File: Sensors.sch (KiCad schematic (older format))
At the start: 66 parts, among them U1 MPXH6250A, U6 SP720

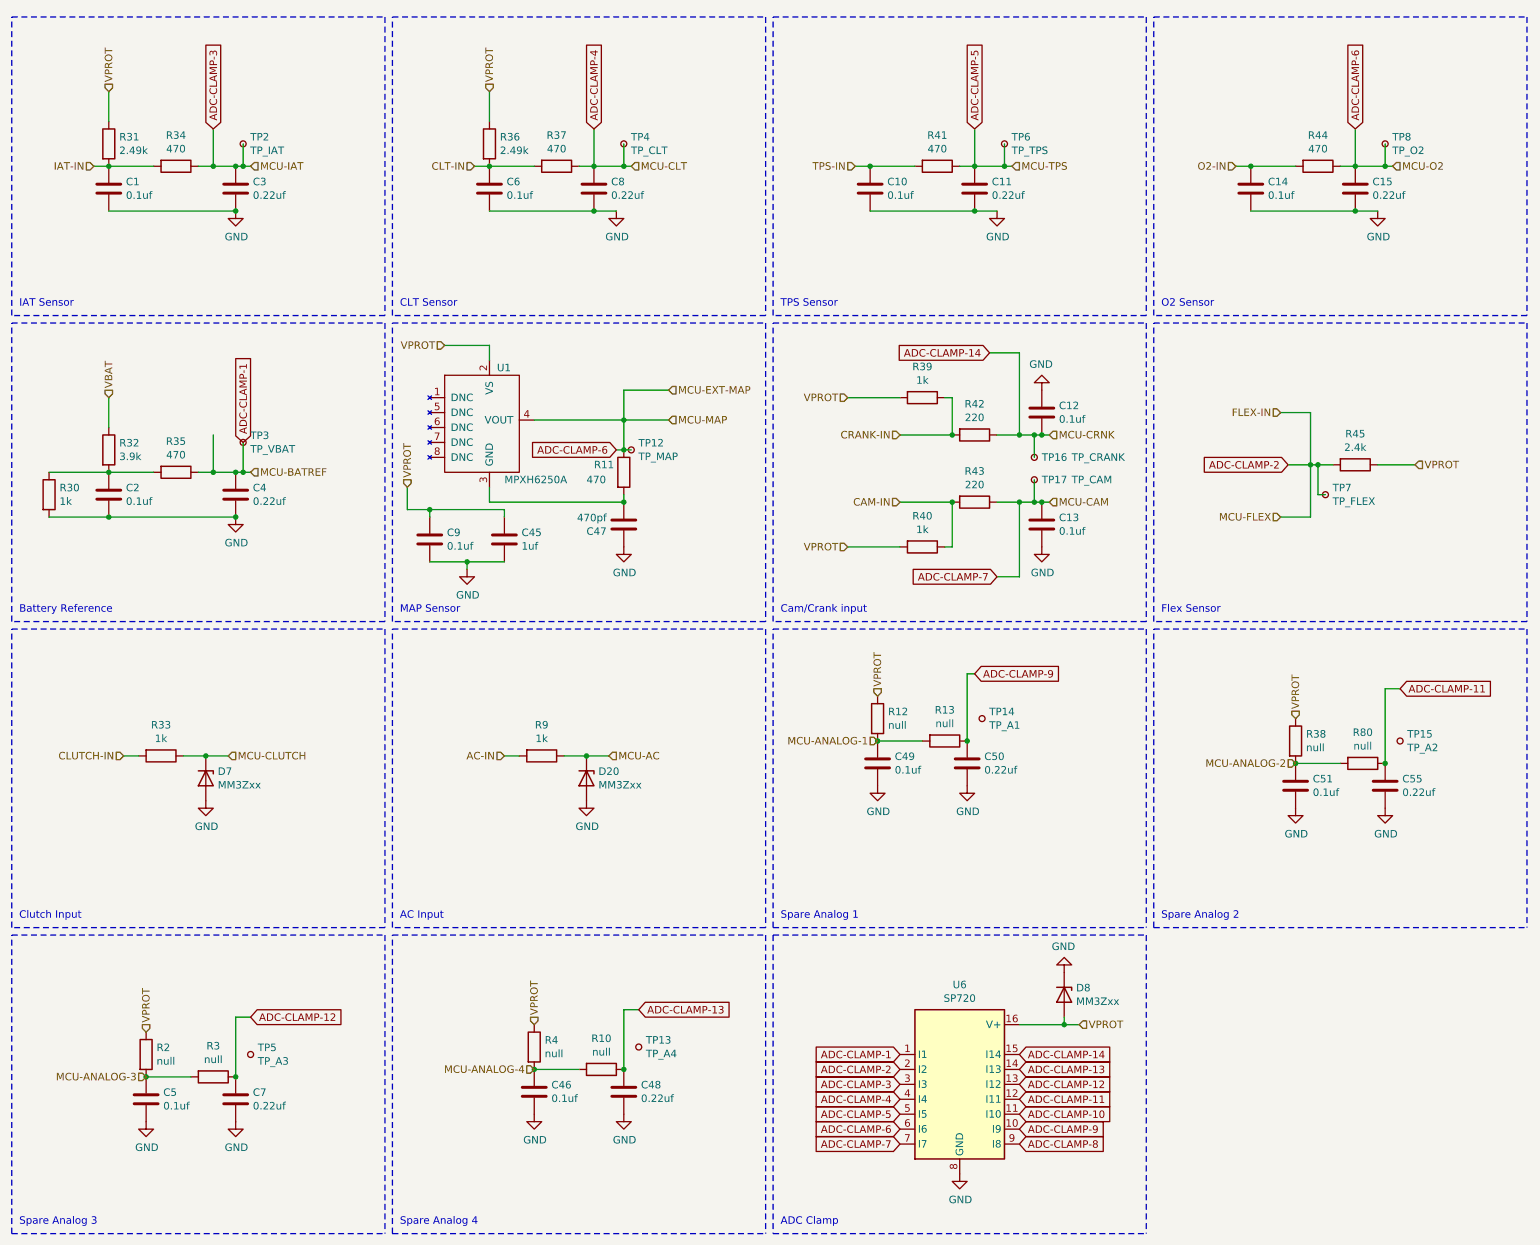
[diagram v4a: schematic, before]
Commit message: Layout checkpoint: everything fits on the board
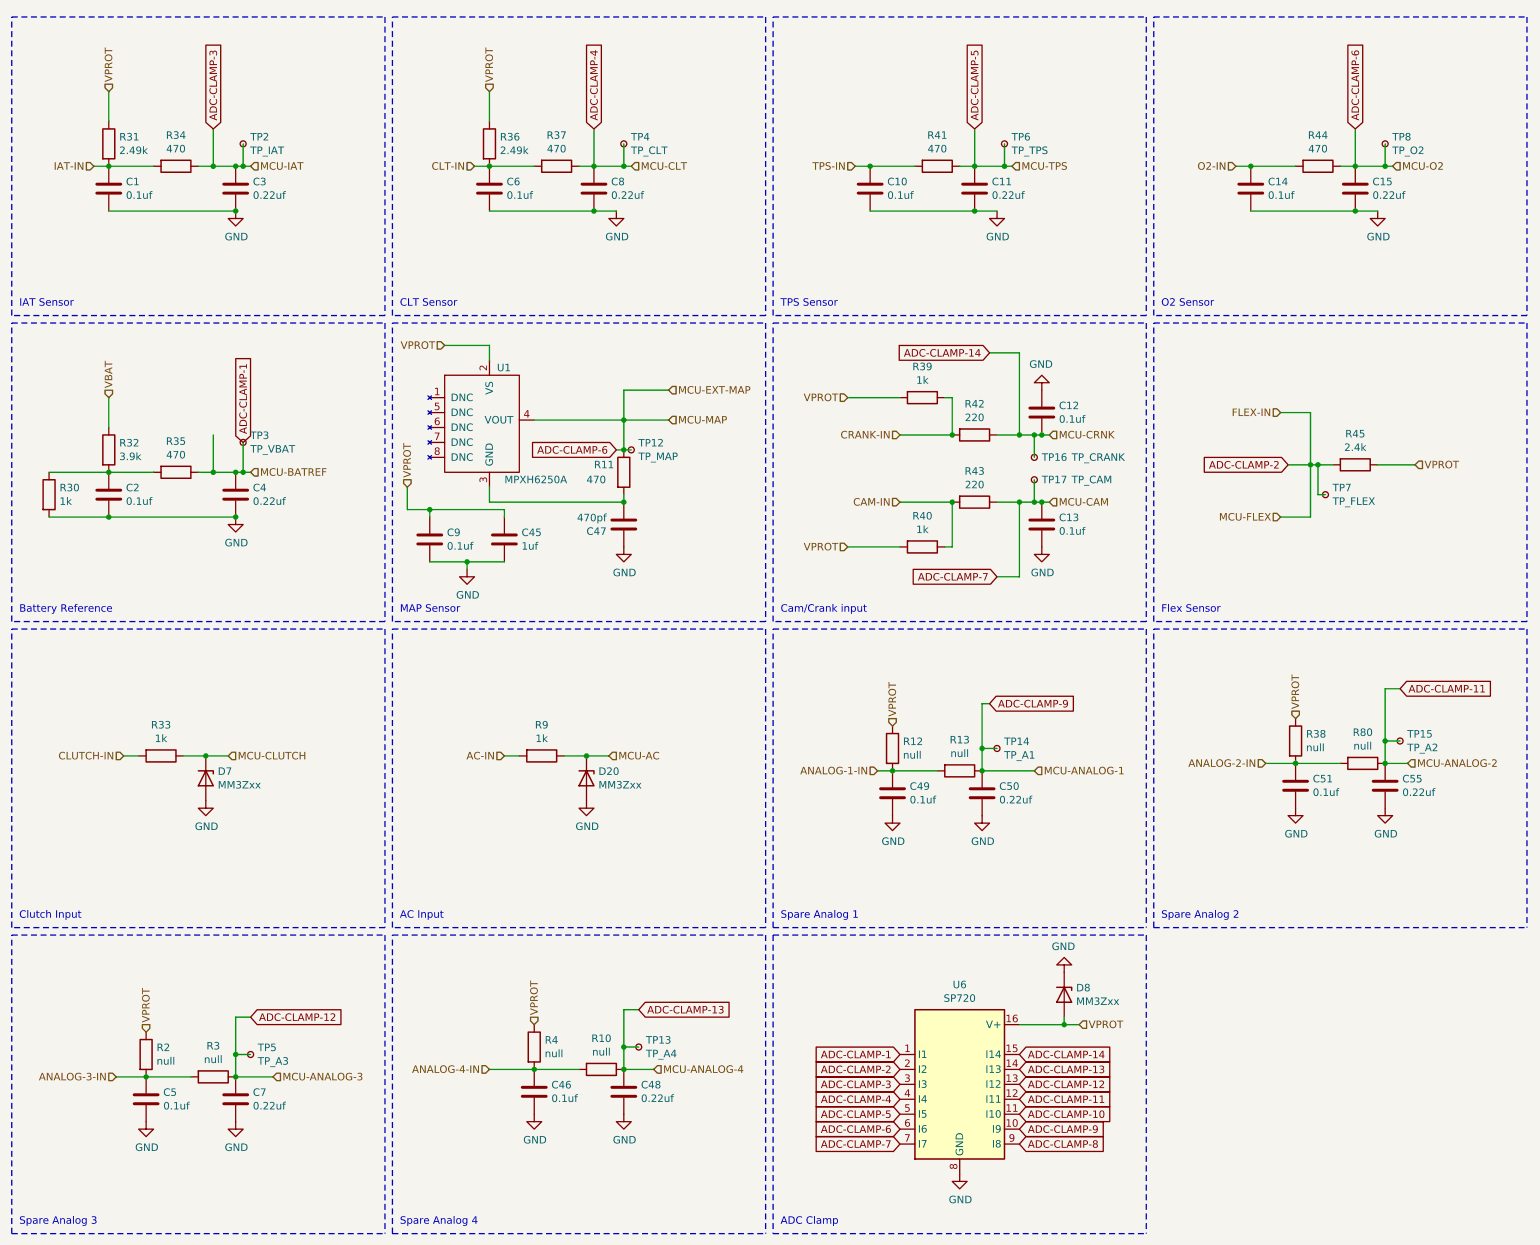
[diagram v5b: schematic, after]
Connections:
- net ADC-CLAMP-11: now also TP15.1
- net ADC-CLAMP-12: now also TP5.1
- net ADC-CLAMP-13: now also TP13.1
- net ADC-CLAMP-9: now also TP14.1
- net MCU-ANALOG-1 renamed ANALOG-1-IN
- net MCU-ANALOG-2 renamed ANALOG-2-IN
- net MCU-ANALOG-3 renamed ANALOG-3-IN
- net MCU-ANALOG-4 renamed ANALOG-4-IN
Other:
- moved on the sheet: C49, C50, R12, R13, TP14
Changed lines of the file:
@@
 Text HLabel 6450 3750 0    50   Input ~ 0
 CAM-IN
-Text GLabel 6950 4900 2    50   Input ~ 0
+Text GLabel 7050 5100 2    50   Input ~ 0
 ADC-CLAMP-9
 Text HLabel 7450 3750 2    50   Input ~ 0
@@
 Wire Notes Line
 	5600 6650 8100 6650
-Text HLabel 6300 5050 1    50   Input ~ 0
+Text HLabel 6400 5250 1    50   Input ~ 0
 VPROT
 $Comp
 L Device:R R12
 U 1 1 61DD1503
-P 6300 5200
-F 0 "R12" H 6370 5246 50  0000 L CNN
-F 1 "null" H 6370 5155 50  0000 L CNN
-F 2 "Resistor_SMD:R_0805_2012Metric_Pad1.20x1.40mm_HandSolder" V 6230 5200 50  0001 C CNN
-F 3 "~" H 6300 5200 50  0001 C CNN
-F 4 "YAG1854CT-ND" H 6300 5200 50  0001 C CNN "DIGIKEY"
-F 5 "C21237" H 6300 5200 50  0001 C CNN "LCSC_PN"
-F 6 "0805" H 6300 5200 50  0001 C CNN "LCSC_FP"
-	1    6300 5200
+P 6400 5400
+F 0 "R12" H 6470 5446 50  0000 L CNN
+F 1 "null" H 6470 5355 50  0000 L CNN
+F 2 "Resistor_SMD:R_0805_2012Metric_Pad1.20x1.40mm_HandSolder" V 6330 5400 50  0001 C CNN
+F 3 "~" H 6400 5400 50  0001 C CNN
+F 4 "YAG1854CT-ND" H 6400 5400 50  0001 C CNN "DIGIKEY"
+F 5 "C21237" H 6400 5400 50  0001 C CNN "LCSC_PN"
+F 6 "0805" H 6400 5400 50  0001 C CNN "LCSC_FP"
+	1    6400 5400
 	1    0    0    -1
 $EndComp
@@
 L Device:C C?
 U 1 1 61DD56EB
-P 6300 5500
+P 6400 5700
 AR Path="/5F2F8F45/61DD56EB" Ref="C?"  Part="1"
 AR Path="/5EFFD74E/61DD56EB" Ref="C49"  Part="1"
-F 0 "C49" H 6415 5546 50  0000 L CNN
-F 1 "0.1uf" H 6415 5455 50  0000 L CNN
-F 2 "Capacitor_SMD:C_0805_2012Metric_Pad1.18x1.45mm_HandSolder" H 6338 5350 50  0001 C CNN
-F 3 "https://datasheet.lcsc.com/szlcsc/YAGEO-CC0805KRX7R9BB104_C49678.pdf" H 6300 5500 50  0001 C CNN
-F 4 "311-1140-1-ND" H 6300 5500 50  0001 C CNN "DIGIKEY"
-F 5 "603-CC805KRX7R9BB104" H 6300 5500 50  0001 C CNN "MOUSER"
-F 6 "C49678" H 6300 5500 50  0001 C CNN "LCSC_PN"
-F 7 "0805" H 6300 5500 50  0001 C CNN "LCSC_FP"
-	1    6300 5500
+F 0 "C49" H 6515 5746 50  0000 L CNN
+F 1 "0.1uf" H 6515 5655 50  0000 L CNN
+F 2 "Capacitor_SMD:C_0805_2012Metric_Pad1.18x1.45mm_HandSolder" H 6438 5550 50  0001 C CNN
+F 3 "https://datasheet.lcsc.com/szlcsc/YAGEO-CC0805KRX7R9BB104_C49678.pdf" H 6400 5700 50  0001 C CNN
+F 4 "311-1140-1-ND" H 6400 5700 50  0001 C CNN "DIGIKEY"
+F 5 "603-CC805KRX7R9BB104" H 6400 5700 50  0001 C CNN "MOUSER"
+F 6 "C49678" H 6400 5700 50  0001 C CNN "LCSC_PN"
+F 7 "0805" H 6400 5700 50  0001 C CNN "LCSC_FP"
+	1    6400 5700
 	1    0    0    -1
 $EndComp
@@
 L Device:R R13
 U 1 1 61DD95EE
-P 6750 5350
-F 0 "R13" V 6543 5350 50  0000 C CNN
-F 1 "null" V 6634 5350 50  0000 C CNN
-F 2 "Resistor_SMD:R_0805_2012Metric_Pad1.20x1.40mm_HandSolder" V 6680 5350 50  0001 C CNN
-F 3 "~" H 6750 5350 50  0001 C CNN
-F 4 "P470CCT-ND" V 6750 5350 50  0001 C CNN "DIGIKEY"
-F 5 "C17710" V 6750 5350 50  0001 C CNN "LCSC_PN"
-F 6 "0805" V 6750 5350 50  0001 C CNN "LCSC_FP"
-	1    6750 5350
+P 6850 5550
+F 0 "R13" V 6643 5550 50  0000 C CNN
+F 1 "null" V 6734 5550 50  0000 C CNN
+F 2 "Resistor_SMD:R_0805_2012Metric_Pad1.20x1.40mm_HandSolder" V 6780 5550 50  0001 C CNN
+F 3 "~" H 6850 5550 50  0001 C CNN
+F 4 "P470CCT-ND" V 6850 5550 50  0001 C CNN "DIGIKEY"
+F 5 "C17710" V 6850 5550 50  0001 C CNN "LCSC_PN"
+F 6 "0805" V 6850 5550 50  0001 C CNN "LCSC_FP"
+	1    6850 5550
 	0    1    1    0
 $EndComp
@@
 L Device:C C50
 U 1 1 61DDE5C4
-P 6900 5500
-F 0 "C50" H 7015 5546 50  0000 L CNN
-F 1 "0.22uf" H 7015 5455 50  0000 L CNN
-F 2 "Capacitor_SMD:C_0805_2012Metric_Pad1.18x1.45mm_HandSolder" H 6938 5350 50  0001 C CNN
-F 3 "~" H 6900 5500 50  0001 C CNN
-F 4 "1276-1284-1-ND" H 6900 5500 50  0001 C CNN "DIGIKEY"
-F 5 "C5378" H 6900 5500 50  0001 C CNN "LCSC_PN"
-F 6 "0805" H 6900 5500 50  0001 C CNN "LCSC_FP"
-	1    6900 5500
-	1    0    0    -1
-$EndComp
-Wire Wire Line
-	6600 5350 6300 5350
-Connection ~ 6300 5350
-Text HLabel 6300 5350 0    50   Input ~ 0
+P 7000 5700
+F 0 "C50" H 7115 5746 50  0000 L CNN
+F 1 "0.22uf" H 7115 5655 50  0000 L CNN
+F 2 "Capacitor_SMD:C_0805_2012Metric_Pad1.18x1.45mm_HandSolder" H 7038 5550 50  0001 C CNN
+F 3 "~" H 7000 5700 50  0001 C CNN
+F 4 "1276-1284-1-ND" H 7000 5700 50  0001 C CNN "DIGIKEY"
+F 5 "C5378" H 7000 5700 50  0001 C CNN "LCSC_PN"
+F 6 "0805" H 7000 5700 50  0001 C CNN "LCSC_FP"
+	1    7000 5700
+	1    0    0    -1
+$EndComp
+Wire Wire Line
+	6700 5550 6400 5550
+Connection ~ 6400 5550
+Text HLabel 7350 5550 2    50   Input ~ 0
 MCU-ANALOG-1
 $Comp
 L power:GND #PWR033
 U 1 1 61DF4E3D
-P 6300 5650
-F 0 "#PWR033" H 6300 5400 50  0001 C CNN
-F 1 "GND" H 6305 5477 50  0000 C CNN
-F 2 "" H 6300 5650 50  0001 C CNN
-F 3 "" H 6300 5650 50  0001 C CNN
-	1    6300 5650
+P 6400 5850
+F 0 "#PWR033" H 6400 5600 50  0001 C CNN
+F 1 "GND" H 6405 5677 50  0000 C CNN
+F 2 "" H 6400 5850 50  0001 C CNN
+F 3 "" H 6400 5850 50  0001 C CNN
+	1    6400 5850
 	1    0    0    -1
 $EndComp
@@
 L power:GND #PWR055
 U 1 1 61DF51AD
-P 6900 5650
-F 0 "#PWR055" H 6900 5400 50  0001 C CNN
-F 1 "GND" H 6905 5477 50  0000 C CNN
-F 2 "" H 6900 5650 50  0001 C CNN
-F 3 "" H 6900 5650 50  0001 C CNN
-	1    6900 5650
+P 7000 5850
+F 0 "#PWR055" H 7000 5600 50  0001 C CNN
+F 1 "GND" H 7005 5677 50  0000 C CNN
+F 2 "" H 7000 5850 50  0001 C CNN
+F 3 "" H 7000 5850 50  0001 C CNN
+	1    7000 5850
 	1    0    0    -1
 $EndComp
@@
 L Connector:TestPoint_Small TP14
 U 1 1 61DF6FD5
-P 7000 5200
-F 0 "TP14" H 7048 5246 50  0000 L CNN
-F 1 "TP_A1" H 7048 5155 50  0000 L CNN
-F 2 "TestPoint:TestPoint_Pad_D1.0mm" H 7200 5200 50  0001 C CNN
-F 3 "~" H 7200 5200 50  0001 C CNN
-	1    7000 5200
+P 7100 5400
+F 0 "TP14" H 7148 5446 50  0000 L CNN
+F 1 "TP_A1" H 7148 5355 50  0000 L CNN
+F 2 "TestPoint:TestPoint_Pad_D1.0mm" H 7300 5400 50  0001 C CNN
+F 3 "~" H 7300 5400 50  0001 C CNN
+	1    7100 5400
 	1    0    0    -1
 $EndComp
@@
 	9400 5500 9100 5500
 Connection ~ 9100 5500
-Text HLabel 9100 5500 0    50   Input ~ 0
+Text HLabel 9850 5500 2    50   Input ~ 0
 MCU-ANALOG-2
 $Comp
@@
 	1700 7600 1400 7600
 Connection ~ 1400 7600
-Text HLabel 1400 7600 0    50   Input ~ 0
+Text HLabel 2250 7600 2    50   Input ~ 0
 MCU-ANALOG-3
 $Comp
@@
 	4300 7550 4000 7550
 Connection ~ 4000 7550
-Text HLabel 4000 7550 0    50   Input ~ 0
+Text HLabel 4800 7550 2    50   Input ~ 0
 MCU-ANALOG-4
 $Comp
@@
 ADC-CLAMP-7
 Wire Wire Line
-	6950 4900 6900 4900
-Wire Wire Line
-	6900 4900 6900 5350
-Connection ~ 6900 5350
+	7050 5100 7000 5100
+Wire Wire Line
+	7000 5100 7000 5400
+Connection ~ 7000 5550
 Text GLabel 9800 5000 2    50   Input ~ 0
 ADC-CLAMP-11
@@
 	9800 5000 9700 5000
 Wire Wire Line
-	9700 5000 9700 5500
+	9700 5000 9700 5350
 Connection ~ 9700 5500
 Text GLabel 2100 7200 2    50   Input ~ 0
@@
 	2100 7200 2000 7200
 Wire Wire Line
-	2000 7200 2000 7600
+	2000 7200 2000 7450
 Connection ~ 2000 7600
 Text GLabel 4700 7150 2    50   Input ~ 0
@@
 	4700 7150 4600 7150
 Wire Wire Line
-	4600 7150 4600 7550
+	4600 7150 4600 7400
 Connection ~ 4600 7550
 Text GLabel 9500 1250 1    50   Input ~ 0
@@
 Text GLabel 7050 2750 0    50   Input ~ 0
 ADC-CLAMP-14
+Wire Wire Line
+	2100 7450 2000 7450
+Connection ~ 2000 7450
+Wire Wire Line
+	2000 7450 2000 7600
+Wire Wire Line
+	2250 7600 2000 7600
+Text HLabel 1200 7600 0    50   Input ~ 0
+ANALOG-3-IN
+Wire Wire Line
+	1200 7600 1400 7600
+Wire Wire Line
+	4700 7400 4600 7400
+Connection ~ 4600 7400
+Wire Wire Line
+	4600 7400 4600 7550
+Wire Wire Line
+	4600 7550 4800 7550
+Text HLabel 3700 7550 0    50   Input ~ 0
+ANALOG-4-IN
+Wire Wire Line
+	3700 7550 4000 7550
+Wire Wire Line
+	7350 5550 7000 5550
+Wire Wire Line
+	7000 5400 7100 5400
+Connection ~ 7000 5400
+Wire Wire Line
+	7000 5400 7000 5550
+Text HLabel 6300 5550 0    50   Input ~ 0
+ANALOG-1-IN
+Wire Wire Line
+	6300 5550 6400 5550
+Wire Wire Line
+	9700 5500 9850 5500
+Wire Wire Line
+	9800 5350 9700 5350
+Connection ~ 9700 5350
+Wire Wire Line
+	9700 5350 9700 5500
+Text HLabel 8900 5500 0    50   Input ~ 0
+ANALOG-2-IN
+Wire Wire Line
+	8900 5500 9100 5500
 $EndSCHEMATC

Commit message: Finish reroute again
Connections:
- net ADC-CLAMP-1: now also C50.1, R13.1, TP14.1; no longer C4.1, R35.1, TP3.1
- net ADC-CLAMP-10: now also C8.1, R37.1, TP4.1
- net ADC-CLAMP-11: now also C15.1, R44.1, TP8.1; no longer C55.1, R80.1, TP15.1
- net ADC-CLAMP-12: now also C4.1, R35.1, TP3.1; no longer C7.1, R3.1, TP5.1
- net ADC-CLAMP-13: now also C3.1, R34.1, TP2.1; no longer C48.1, R10.1, TP13.1
- net ADC-CLAMP-14: now also C11.1, R41.1, TP6.1; no longer C12.2, R42.1, TP16.1
- net ADC-CLAMP-2: now also C55.1, R80.1, TP15.1; no longer R45.2, TP7.1
- net ADC-CLAMP-3: now also C7.1, R3.1, TP5.1; no longer C3.1, R34.1, TP2.1
- net ADC-CLAMP-4: now also C48.1, R10.1, TP13.1; no longer C8.1, R37.1, TP4.1
- net ADC-CLAMP-5: now also C12.2, R42.1, TP16.1; no longer C11.1, R41.1, TP6.1
- net ADC-CLAMP-6: now also C13.1, R43.1, TP17.1; no longer C15.1, R11.1, R44.1, TP12.1, TP8.1, U1.4 (VOUT)
- net ADC-CLAMP-7: now also R45.2, TP7.1; no longer C13.1, R43.1, TP17.1
- net ADC-CLAMP-9: now also R11.1, TP12.1, U1.4 (VOUT); no longer C50.1, R13.1, TP14.1
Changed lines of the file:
@@
 Text GLabel 6450 7450 0    50   Input ~ 0
 ADC-CLAMP-1
-Text GLabel 2050 3350 1    50   Input ~ 0
-ADC-CLAMP-1
+Text GLabel 1850 3300 1    50   Input ~ 0
+ADC-CLAMP-12
 Wire Wire Line
 	1850 1250 1850 1500
@@
 	4300 1500 4400 1500
 Text GLabel 9050 3500 0    50   Input ~ 0
-ADC-CLAMP-2
+ADC-CLAMP-7
 Wire Wire Line
 	4400 1250 4400 1500
@@
 	6850 1500 6950 1500
 Text GLabel 1850 1250 1    50   Input ~ 0
-ADC-CLAMP-3
+ADC-CLAMP-13
 Wire Wire Line
 	6950 1250 6950 1500
@@
 	9400 1500 9500 1500
 Text GLabel 4400 1250 1    50   Input ~ 0
-ADC-CLAMP-4
+ADC-CLAMP-10
 Wire Wire Line
 	9500 1250 9500 1500
@@
 	1750 3550 1850 3550
 Text GLabel 6950 1250 1    50   Input ~ 0
-ADC-CLAMP-5
+ADC-CLAMP-14
 Wire Wire Line
 	1850 3300 1850 3550
@@
 Text HLabel 6450 3750 0    50   Input ~ 0
 CAM-IN
-Text GLabel 7050 5100 2    50   Input ~ 0
-ADC-CLAMP-9
 Text HLabel 7450 3750 2    50   Input ~ 0
 MCU-CAM
@@
 F 3 "~" H 7550 3600 50  0001 C CNN
 	1    7350 3600
-	1    0    0    -1
+	1    0    0    1
 $EndComp
 Wire Wire Line
@@
 	4600 3700 4600 3750
 Text GLabel 4550 3400 0    50   Input ~ 0
-ADC-CLAMP-6
+ADC-CLAMP-9
 Text HLabel 4900 3200 2    50   Input ~ 0
 MCU-MAP
@@
 Wire Wire Line
 	4650 3400 4600 3400
-Text HLabel 4900 3000 2    50   Input ~ 0
-MCU-EXT-MAP
 $Comp
 L Device:C C?
@@
 Connection ~ 4600 3200
 Wire Wire Line
-	4900 3000 4600 3000
-Wire Wire Line
-	4600 3000 4600 3200
-Wire Wire Line
 	3400 2700 3700 2700
 Wire Wire Line
@@
 Connection ~ 3300 3800
 Text GLabel 7100 4250 0    50   Input ~ 0
-ADC-CLAMP-7
+ADC-CLAMP-6
 Wire Wire Line
 	7050 5100 7000 5100
@@
 Connection ~ 7000 5550
 Text GLabel 9800 5000 2    50   Input ~ 0
-ADC-CLAMP-11
+ADC-CLAMP-2
 Wire Wire Line
 	9800 5000 9700 5000
@@
 Connection ~ 9700 5500
 Text GLabel 2100 7200 2    50   Input ~ 0
-ADC-CLAMP-12
+ADC-CLAMP-3
 Wire Wire Line
 	2100 7200 2000 7200
@@
 Connection ~ 2000 7600
 Text GLabel 4700 7150 2    50   Input ~ 0
-ADC-CLAMP-13
+ADC-CLAMP-4
 Wire Wire Line
 	4700 7150 4600 7150
@@
 Connection ~ 4600 7550
 Text GLabel 9500 1250 1    50   Input ~ 0
-ADC-CLAMP-6
+ADC-CLAMP-11
 Text GLabel 7050 2750 0    50   Input ~ 0
-ADC-CLAMP-14
+ADC-CLAMP-5
 Wire Wire Line
 	2100 7450 2000 7450
@@
 Wire Wire Line
 	8900 5500 9100 5500
+Text GLabel 7050 5100 2    50   Input ~ 0
+ADC-CLAMP-1
 $EndSCHEMATC

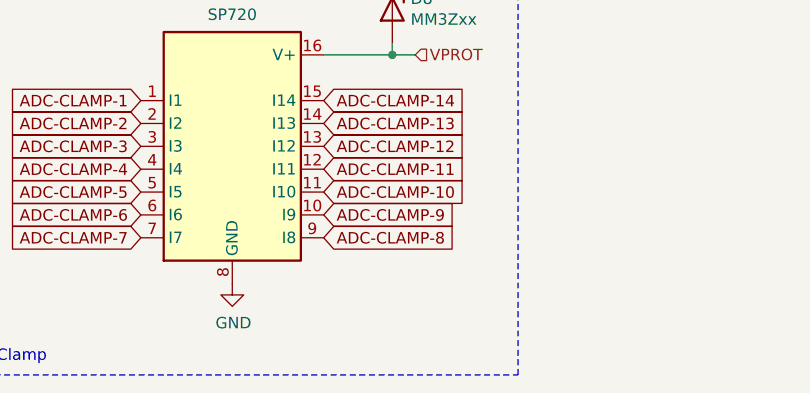
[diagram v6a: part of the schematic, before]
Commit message: Schematic and Layout Updates
* cleanup unused pins for DRC
* swap swd connector for the fancy one the phill uses
* swap out the CAN transciever for one more suitable for 3v3
* reroute CAN differential pair
* clean up copper pours
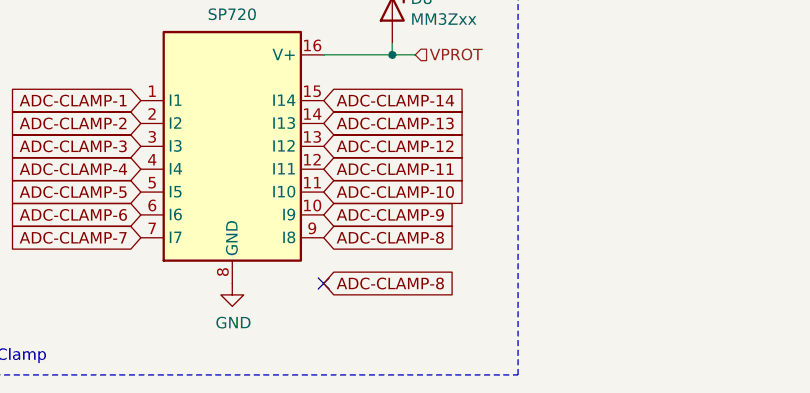
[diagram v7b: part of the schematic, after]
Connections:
- no-connect marks 0 -> 1
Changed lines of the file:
@@
 Text GLabel 7050 5100 2    50   Input ~ 0
 ADC-CLAMP-1
+Text GLabel 7250 8250 2    50   Input ~ 0
+ADC-CLAMP-8
+NoConn ~ 7250 8250
 $EndSCHEMATC
